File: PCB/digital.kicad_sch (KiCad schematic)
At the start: 29 parts, among them J14 FINAL_CARRERA_UP, J15 FINAL_CARRERA_DOWN, J3 ICSP, J4 CAN, J6 USART, J7 SPI, J8 RFID_COAX, U2 PIC32MK0256MCJ048-I/Y8X, U3 TCAN334D, Y1 ASZKDV-32.768KHZ-L-T3, Y2 ECS-3225SMV-080-GP-TR

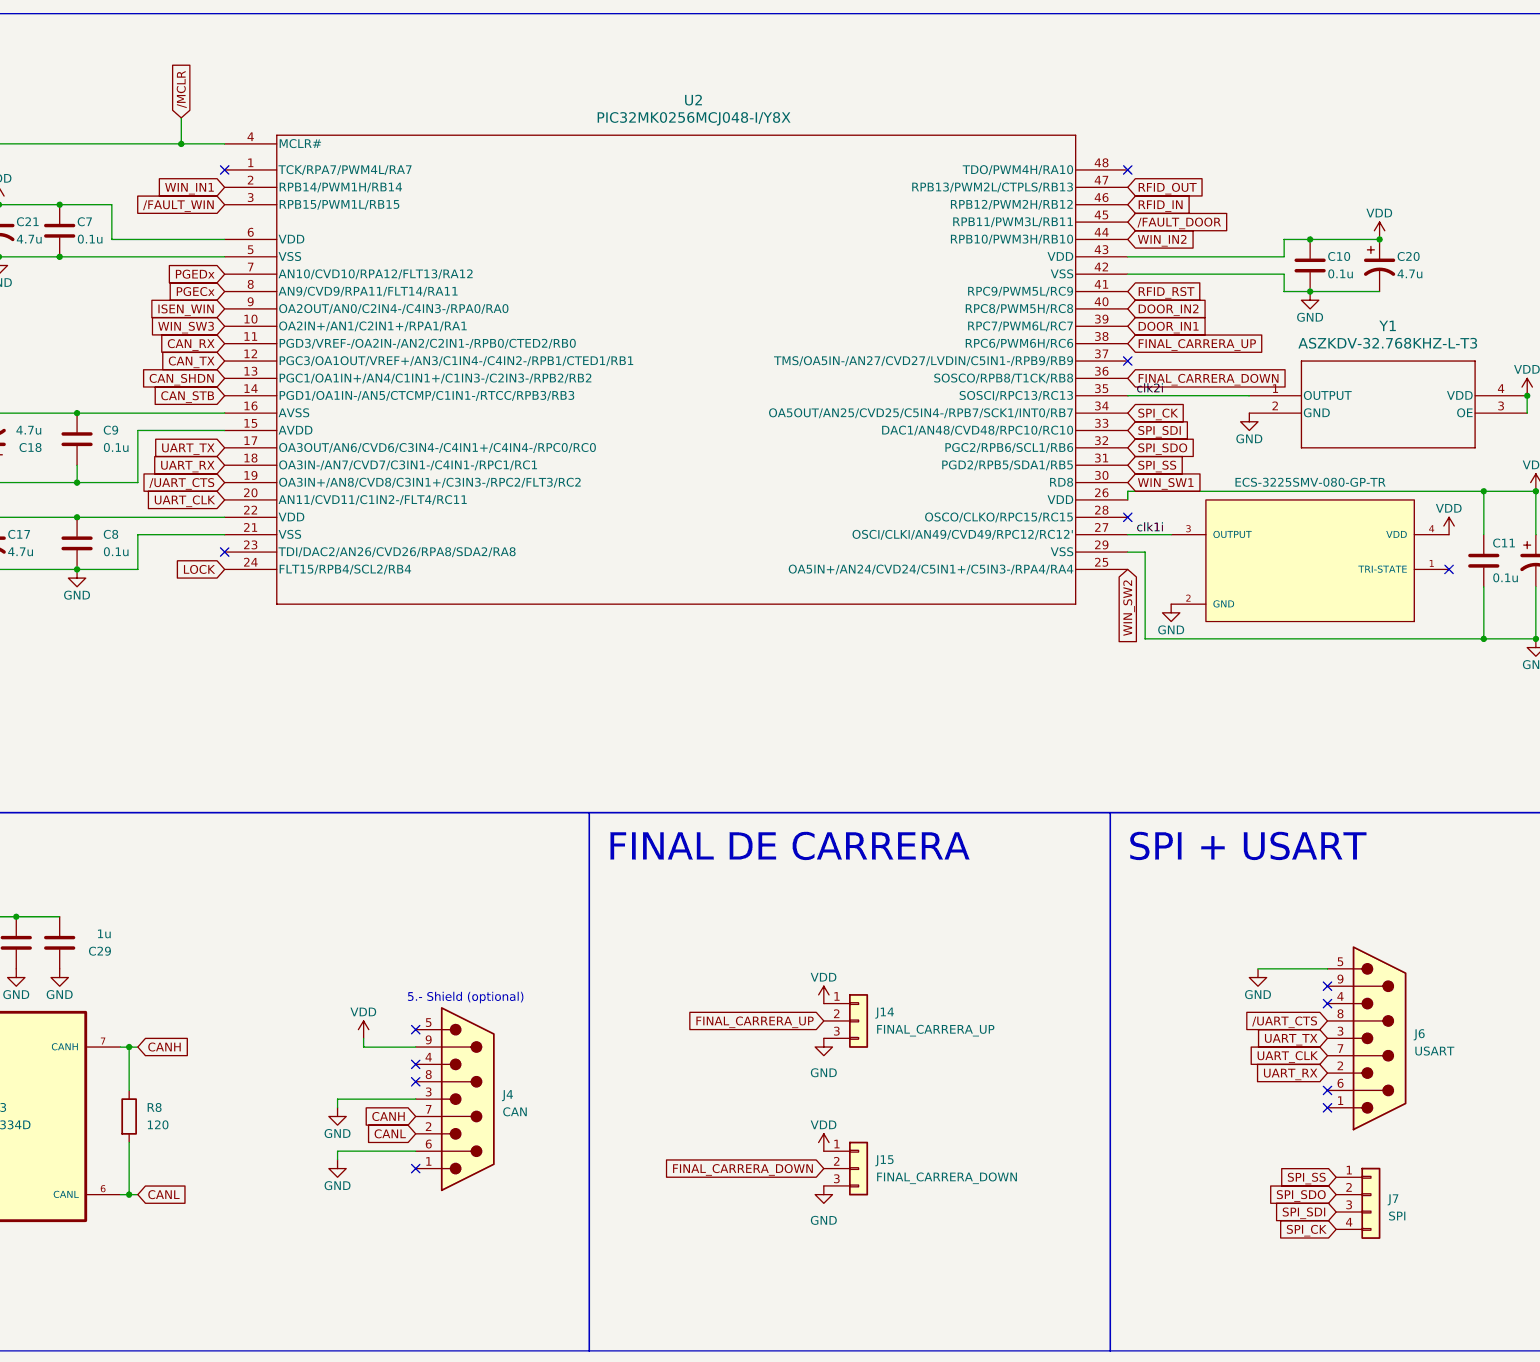
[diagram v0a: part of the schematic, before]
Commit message: PCB LAYOUT 2.0 - rearranged uc pins, changed smd Cs to ceramic
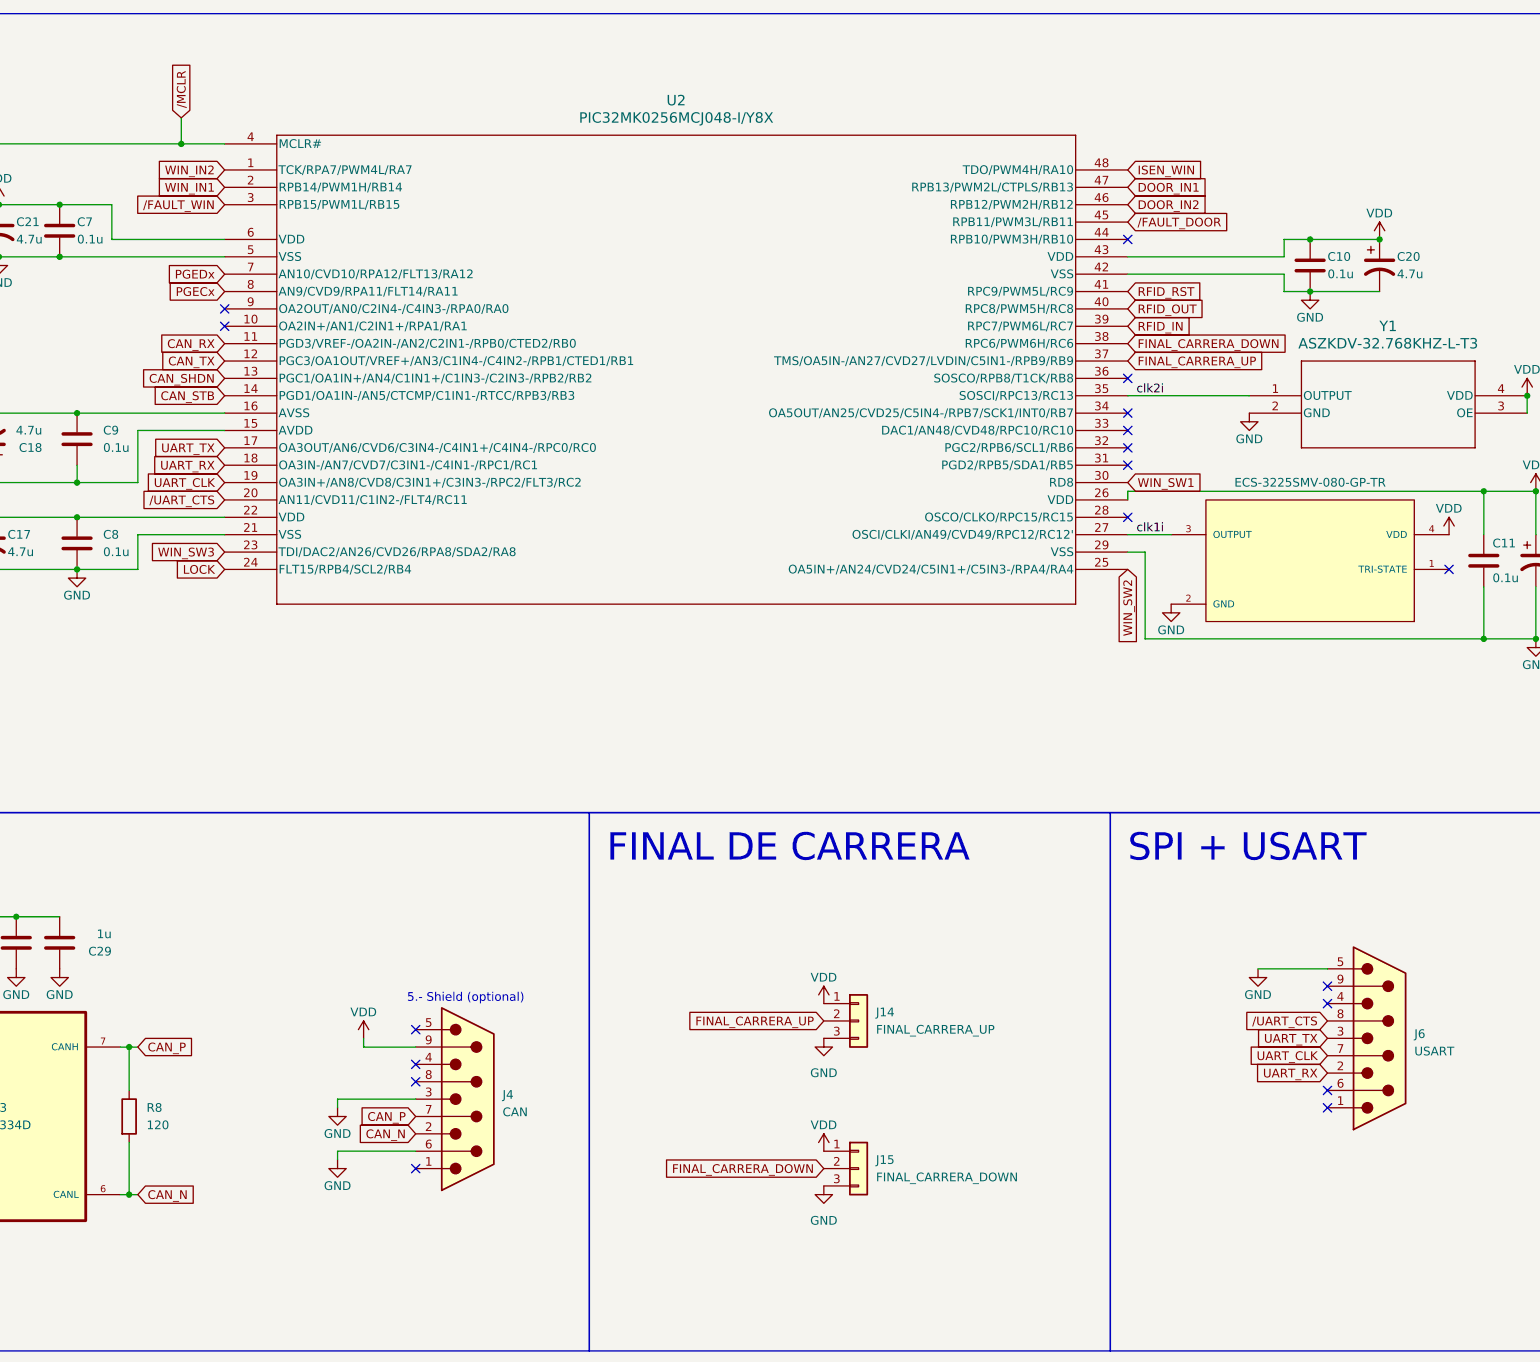
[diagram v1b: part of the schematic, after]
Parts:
- removed J7: SPI, TerminalBlock_MetzConnect:TerminalBlock_MetzConnect_Type011_RT05504HBWC_1x04_P5.00mm_Horizontal, symbol Connector_Generic:Conn_01x04
- C10, C11, C12, C14, C28, C29, C7, C8, C9: footprint Capacitor_SMD:C_0805_2012Metric -> Capacitor_SMD:C_0402_1005Metric
- C17, C18, C19, C20, C21: footprint kicad_models:CAPAE430X550N -> Capacitor_SMD:C_0805_2012Metric
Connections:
- net DOOR_IN1: now also U2.47 (RPB13/PWM2L/CTPLS/RB13); no longer U2.39 (RPC7/PWM6L/RC7)
- net DOOR_IN2: now also U2.46 (RPB12/PWM2H/RB12); no longer U2.40 (RPC8/PWM5H/RC8)
- net FINAL_CARRERA_DOWN: now also U2.38 (RPC6/PWM6H/RC6); no longer U2.36 (SOSCO/RPB8/T1CK/RB8)
- net FINAL_CARRERA_UP: now also U2.37 (TMS/OA5IN-/AN27/CVD27/LVDIN/C5IN1-/RPB9/RB9); no longer U2.38 (RPC6/PWM6H/RC6)
- net ISEN_WIN: now also U2.48 (TDO/PWM4H/RA10); no longer U2.9 (OA2OUT/AN0/C2IN4-/C4IN3-/RPA0/RA0)
- net RFID_IN: now also U2.39 (RPC7/PWM6L/RC7); no longer U2.46 (RPB12/PWM2H/RB12)
- net RFID_OUT: now also U2.40 (RPC8/PWM5H/RC8); no longer U2.47 (RPB13/PWM2L/CTPLS/RB13)
- net UART_CLK: now also U2.19 (OA3IN+/AN8/CVD8/C3IN1+/C3IN3-/RPC2/FLT3/RC2); no longer U2.20 (AN11/CVD11/C1IN2-/FLT4/RC11)
- net WIN_IN2: now also U2.1 (TCK/RPA7/PWM4L/RA7); no longer U2.44 (RPB10/PWM3H/RB10)
- net WIN_SW3: now also U2.23 (TDI/DAC2/AN26/CVD26/RPA8/SDA2/RA8); no longer U2.10 (OA2IN+/AN1/C2IN1+/RPA1/RA1)
- net /UART_CTS: now also U2.20 (AN11/CVD11/C1IN2-/FLT4/RC11); no longer U2.19 (OA3IN+/AN8/CVD8/C3IN1+/C3IN3-/RPC2/FLT3/RC2)
- net CANH renamed CAN_P
- net CANL renamed CAN_N
- net SPI_CK: no longer names the net of U2.34 (OA5OUT/AN25/CVD25/C5IN4-/RPB7/SCK1/INT0/RB7)
- net SPI_SDI: no longer names the net of U2.33 (DAC1/AN48/CVD48/RPC10/RC10)
- net SPI_SDO: no longer names the net of U2.32 (PGC2/RPB6/SCL1/RB6)
- net SPI_SS: no longer names the net of U2.31 (PGD2/RPB5/SDA1/RB5)
- no-connect marks 19 -> 23

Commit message: complete budget
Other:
- note added: "USART"
- note removed: "SPI + USART"
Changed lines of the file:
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@@
     (effects (font (size 4 4)) (justify left bottom))
   )
-  (text "SPI + USART" (at 217.17 137.16 0)
+  (text "USART" (at 217.17 137.16 0)
     (effects (font (size 4 4)) (justify left bottom))
   )
